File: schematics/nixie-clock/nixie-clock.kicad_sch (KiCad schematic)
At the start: 23 parts, among them J1 Jack-DC, SW1 SW_Push, U1 LM317_TO-220, U2 ATmega328P-P, U3 SN74HC595N, U4 SN74HC595N, U5 K155NA1, U6 K155NA1, U7 K155NA1, U8 K155NA1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

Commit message: annotated nixie driver's inputs
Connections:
- net SER2: now also U3.9 (QH')
- net N1A: now reaches U5.3 (A)
- net N1D: now reaches U5.4 (D)
- net N1B: now reaches U5.6 (B)
- net N1C: now reaches U5.7 (C)
- net N3A: now reaches U7.3 (A)
- net N3D: now reaches U7.4 (D)
- net N3B: now reaches U7.6 (B)
- net N3C: now reaches U7.7 (C)
- net N2A: now reaches U6.3 (A)
- net N2D: now reaches U6.4 (D)
- net N2B: now reaches U6.6 (B)
- net N2C: now reaches U6.7 (C)
- net N4A: now reaches U8.3 (A)
- net N4D: now reaches U8.4 (D)
- net N4B: now reaches U8.6 (B)
- net N4C: now reaches U8.7 (C)
- no-connect marks 0 -> 3
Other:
- note added: "5V Voltage regulator"
- note added: "Crystal oscillator"
- note added: "DC Connector"
- note added: "Nixie tubes and driver circuits"
- note added: "Reset button"
- moved on the sheet: BZ1, C1, C2, C3, C4, J1, N1, N2, N3, N4, R1, R2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

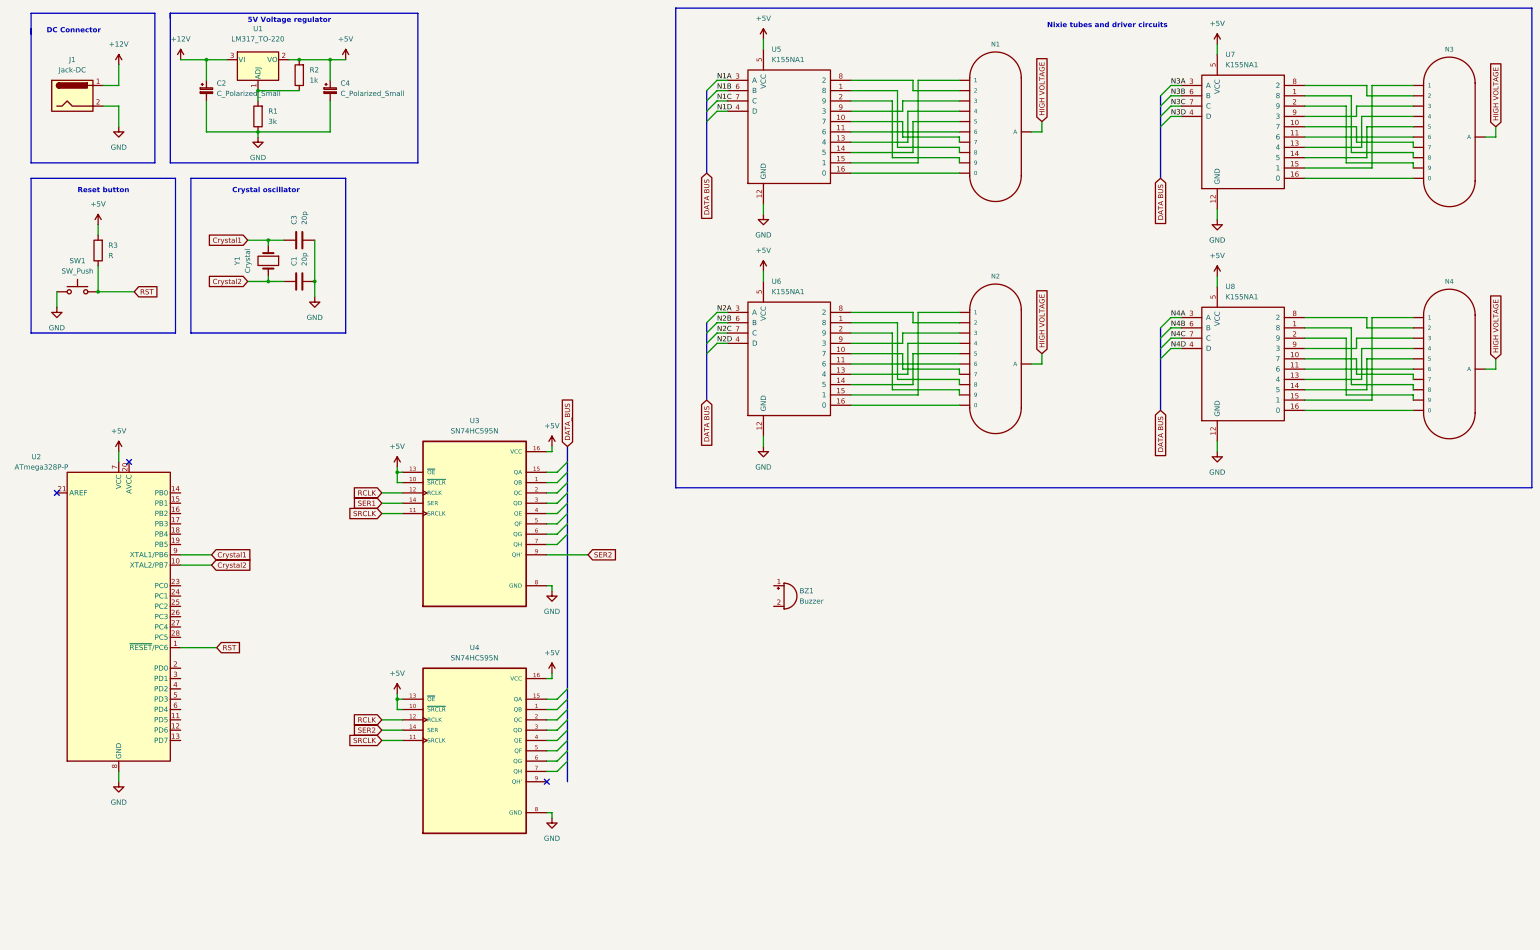
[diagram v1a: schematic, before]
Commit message: schematic: added buttons, rtc, neon bulbs, annotated driver input labels
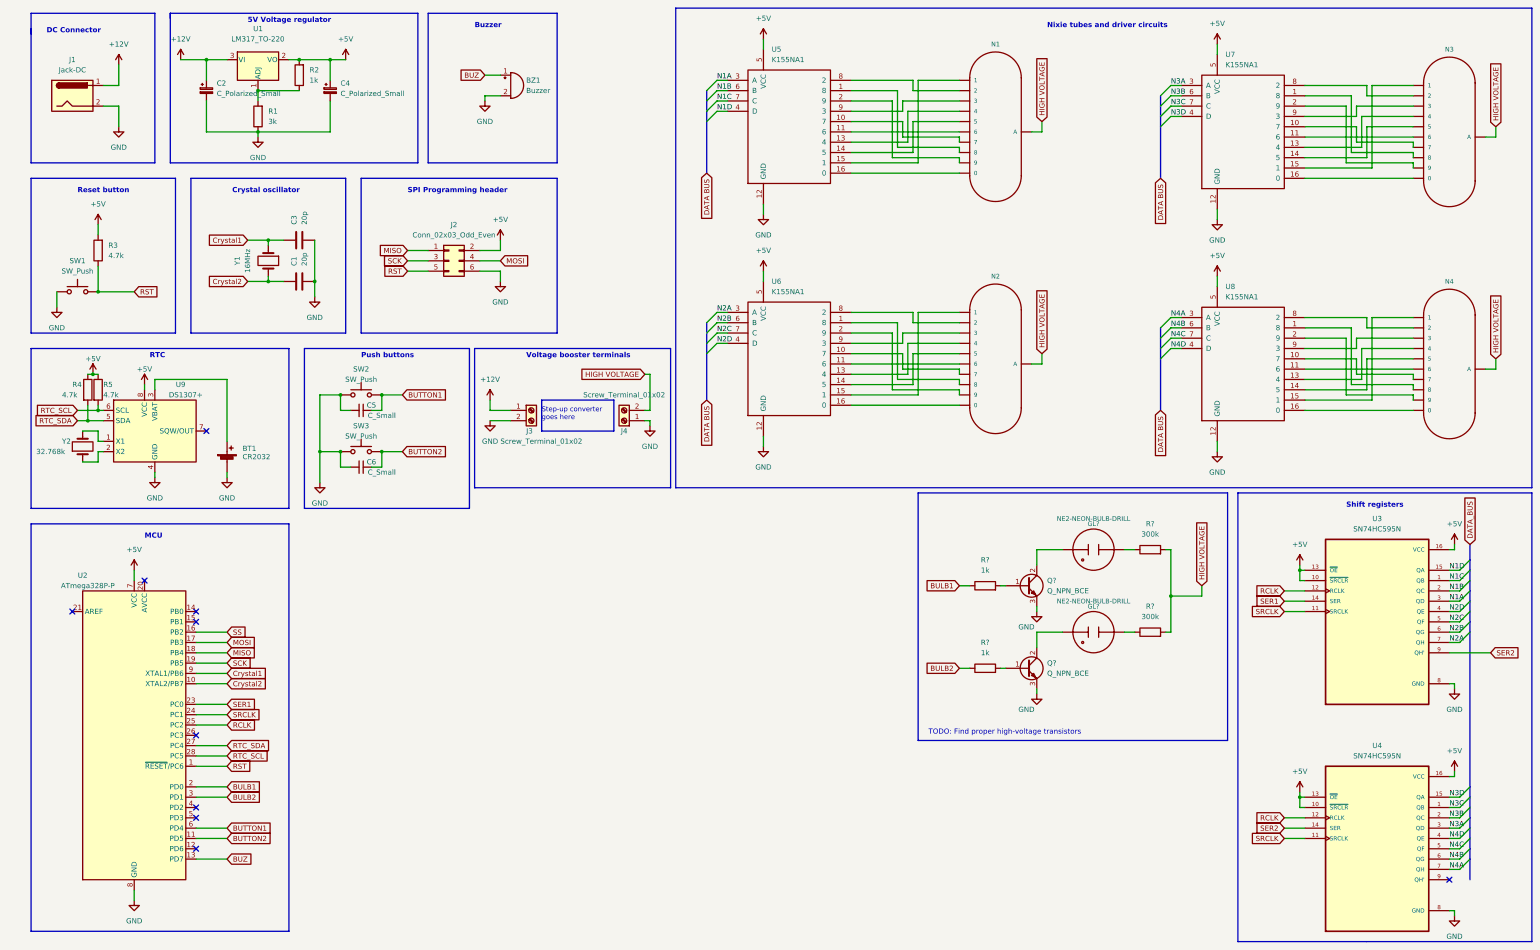
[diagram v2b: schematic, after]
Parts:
- added BT1: CR2032, symbol Device:Battery_Cell
- added C5, C6: C_Small, symbol Device:C_Small
- added GL? (x2): NE2-NEON-BULB-DRILL, mynixies_NE2-NEON-BULB-DRILL, symbol mynixies:NE2-NEON-BULB-DRILL
- added J2: Conn_02x03_Odd_Even, Connector_PinHeader_2.54mm:PinHeader_2x03_P2.54mm_Vertical, symbol Connector_Generic:Conn_02x03_Odd_Even
- added J3, J4: Screw_Terminal_01x02, symbol Connector:Screw_Terminal_01x02
- added Q? (x2): Q_NPN_BCE, symbol Device:Q_NPN_BCE
- added R4, R5: 4.7k, symbol Device:R
- added R? (x2): 1k, symbol Device:R
- added R? (x2): 300k, symbol Device:R
- added SW2, SW3: SW_Push, symbol Switch:SW_Push
- added U9: DS1307+, Package_DIP:DIP-8_W7.62mm, symbol Timer_RTC:DS1307+
- added Y2: 32.768k, symbol Device:Crystal
- N1: footprint nixies-us_IN-1 -> (none)
- R3: value R -> 4.7k
- U5, U6, U7, U8: footprint (none) -> Package_DIP:DIP-14_W7.62mm_Socket
- Y1: value Crystal -> 16MHz
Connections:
- net +12V: now also J3.1 (Pin_1)
- net +5V: now also J2.2 (Pin_2), R4.1, R5.1, U9.8 (VCC)
- net GND: now also BZ1.2 (+), BT1.2 (-), C5.2, C6.2, J2.6 (Pin_6), J3.2 (Pin_2), J4.1 (Pin_1), Q?.3 (E), Q?.3 (E), SW2.1, SW3.1, U9.4 (GND)
- net HIGH VOLTAGE: now also J4.2 (Pin_2), R?.2, R?.2
- net N1A: now also U3.3 (QD)
- net N1B: now also U3.2 (QC)
- net N1C: now also U3.1 (QB)
- net N1D: now also U3.15 (QA)
- net N2A: now also U3.7 (QH)
- net N2B: now also U3.6 (QG)
- net N2C: now also U3.5 (QF)
- net N2D: now also U3.4 (QE)
- net N3A: now also U4.3 (QD)
- net N3B: now also U4.2 (QC)
- net N3C: now also U4.1 (QB)
- net N3D: now also U4.15 (QA)
- net N4A: now also U4.7 (QH)
- net N4B: now also U4.6 (QG)
- net N4C: now also U4.5 (QF)
- net N4D: now also U4.4 (QE)
- net RCLK: now also U2.25 (PC2)
- net RST: now also J2.5 (Pin_5)
- net SER1: now also U2.23 (PC0)
- net SRCLK: now also U2.24 (PC1)
- net BUZ: now reaches BZ1.1 (-)
- net BUZ: now also U2.13 (PD7)
- net BUTTON2: now reaches U2.11 (PD5)
- net BUTTON2: now also C6.1, SW3.2
- net SS: now reaches U2.16 (PB2)
- net MOSI: now reaches U2.17 (PB3)
- net MOSI: now also J2.4 (Pin_4)
- net MISO: now reaches U2.18 (PB4)
- net MISO: now also J2.1 (Pin_1)
- net SCK: now reaches U2.19 (PB5)
- net SCK: now also J2.3 (Pin_3)
- net BULB1: now reaches U2.2 (PD0)
- net BULB1: now also R?.1
- net RTC_SDA: now reaches U2.27 (PC4)
- net RTC_SDA: now also R4.2, U9.5 (SDA)
- net RTC_SCL: now reaches U2.28 (PC5)
- net RTC_SCL: now also R5.2, U9.6 (SCL)
- net BULB2: now reaches U2.3 (PD1)
- net BULB2: now also R?.1
- net BUTTON1: now reaches U2.6 (PD4)
- net BUTTON1: now also C5.1, SW2.2
- new net: BT1.1 (+), U9.3 (VBAT)
- new net: Q?.1 (B), R?.2 (x2)
- new net: GL?.1 (A), R?.1 (x2)
- new net: GL?.2 (A1), Q?.2 (C) (x2)
- new net: U9.1 (X1), Y2.2
- new net: U9.2 (X2), Y2.1
- no-connect marks 3 -> 10
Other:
- note added: "Buzzer"
- note added: "MCU"
- note added: "Push buttons"
- note added: "RTC"
- note added: "SPI Programming header"
- note added: "Shift registers"
- note added: "Step-up converter goes here"
- note added: "TODO: Find proper high-voltage transistors"
- note added: "Voltage booster terminals"
- moved on the sheet: BZ1, U2, U3, U4

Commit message: schematic: corrected k155id1's pinout to dip16 instead of 14
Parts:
- GL? (x2): value NE2-NEON-BULB-DRILL -> INS-1
- U5, U6, U7, U8: value K155NA1 -> K155ID1; footprint Package_DIP:DIP-14_W7.62mm_Socket -> Package_DIP:DIP-16_W7.62mm_Socket
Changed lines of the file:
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@@
       (effects (font (size 1.27 1.27)) (justify left))
     )
-    (property "Value" "K155NA1" (id 1) (at 207.7594 34.29 0)
-      (effects (font (size 1.27 1.27)) (justify left))
-    )
-    (property "Footprint" "Package_DIP:DIP-14_W7.62mm_Socket" (id 2) (at 212.09 50.8 0)
+    (property "Value" "K155ID1" (id 1) (at 207.7594 34.29 0)
+      (effects (font (size 1.27 1.27)) (justify left))
+    )
+    (property "Footprint" "Package_DIP:DIP-16_W7.62mm_Socket" (id 2) (at 212.09 50.8 0)
       (effects (font (size 1.27 1.27)) hide)
     )
@@
       (effects (font (size 1.143 1.143)))
     )
-    (property "Value" "NE2-NEON-BULB-DRILL" (id 1) (at 287.02 147.32 90)
+    (property "Value" "INS-1" (id 1) (at 287.02 161.29 90)
       (effects (font (size 1.143 1.143)))
     )
@@
       (effects (font (size 1.27 1.27)) (justify left))
     )
-    (property "Value" "K155NA1" (id 1) (at 319.5194 35.56 0)
-      (effects (font (size 1.27 1.27)) (justify left))
-    )
-    (property "Footprint" "Package_DIP:DIP-14_W7.62mm_Socket" (id 2) (at 323.85 52.07 0)
+    (property "Value" "K155ID1" (id 1) (at 319.5194 35.56 0)
+      (effects (font (size 1.27 1.27)) (justify left))
+    )
+    (property "Footprint" "Package_DIP:DIP-16_W7.62mm_Socket" (id 2) (at 323.85 52.07 0)
       (effects (font (size 1.27 1.27)) hide)
     )
@@
       (effects (font (size 1.27 1.27)) (justify left))
     )
-    (property "Value" "K155NA1" (id 1) (at 207.7594 91.44 0)
-      (effects (font (size 1.27 1.27)) (justify left))
-    )
-    (property "Footprint" "Package_DIP:DIP-14_W7.62mm_Socket" (id 2) (at 212.09 107.95 0)
+    (property "Value" "K155ID1" (id 1) (at 207.7594 91.44 0)
+      (effects (font (size 1.27 1.27)) (justify left))
+    )
+    (property "Footprint" "Package_DIP:DIP-16_W7.62mm_Socket" (id 2) (at 212.09 107.95 0)
       (effects (font (size 1.27 1.27)) hide)
     )
@@
       (effects (font (size 1.27 1.27)) (justify left))
     )
-    (property "Value" "K155NA1" (id 1) (at 319.5194 92.71 0)
-      (effects (font (size 1.27 1.27)) (justify left))
-    )
-    (property "Footprint" "Package_DIP:DIP-14_W7.62mm_Socket" (id 2) (at 323.85 109.22 0)
+    (property "Value" "K155ID1" (id 1) (at 319.5194 92.71 0)
+      (effects (font (size 1.27 1.27)) (justify left))
+    )
+    (property "Footprint" "Package_DIP:DIP-16_W7.62mm_Socket" (id 2) (at 323.85 109.22 0)
       (effects (font (size 1.27 1.27)) hide)
     )
@@
       (effects (font (size 1.143 1.143)))
     )
-    (property "Value" "NE2-NEON-BULB-DRILL" (id 1) (at 287.02 167.64 90)
+    (property "Value" "INS-1" (id 1) (at 287.02 181.61 90)
       (effects (font (size 1.143 1.143)))
     )
@@
     )
     (path "/345e2975-581d-4a8c-8af1-443eac8fd640"
-      (reference "GL?") (unit 1) (value "NE2-NEON-BULB-DRILL") (footprint "mynixies_NE2-NEON-BULB-DRILL")
+      (reference "GL?") (unit 1) (value "INS-1") (footprint "mynixies_NE2-NEON-BULB-DRILL")
     )
     (path "/fbf9fc96-43f5-4a53-be4f-0f9323bfd90c"
-      (reference "GL?") (unit 1) (value "NE2-NEON-BULB-DRILL") (footprint "mynixies_NE2-NEON-BULB-DRILL")
+      (reference "GL?") (unit 1) (value "INS-1") (footprint "mynixies_NE2-NEON-BULB-DRILL")
     )
     (path "/2f3c2211-6c84-4020-a1b4-5759bcf85a5c"
@@
     )
     (path "/04d182f1-d009-49f3-b3e6-b46d9a90aa92"
-      (reference "U5") (unit 1) (value "K155NA1") (footprint "Package_DIP:DIP-14_W7.62mm_Socket")
+      (reference "U5") (unit 1) (value "K155ID1") (footprint "Package_DIP:DIP-16_W7.62mm_Socket")
     )
     (path "/64e8c480-67c5-45e2-9eb8-ede62713c06f"
-      (reference "U6") (unit 1) (value "K155NA1") (footprint "Package_DIP:DIP-14_W7.62mm_Socket")
+      (reference "U6") (unit 1) (value "K155ID1") (footprint "Package_DIP:DIP-16_W7.62mm_Socket")
     )
     (path "/52613085-5931-49fd-bd52-08509dc07be3"
-      (reference "U7") (unit 1) (value "K155NA1") (footprint "Package_DIP:DIP-14_W7.62mm_Socket")
+      (reference "U7") (unit 1) (value "K155ID1") (footprint "Package_DIP:DIP-16_W7.62mm_Socket")
     )
     (path "/d2a2bba5-d132-4e9e-a70e-8efe18d0ccab"
-      (reference "U8") (unit 1) (value "K155NA1") (footprint "Package_DIP:DIP-14_W7.62mm_Socket")
+      (reference "U8") (unit 1) (value "K155ID1") (footprint "Package_DIP:DIP-16_W7.62mm_Socket")
     )
     (path "/9173ca2e-fc04-4e30-a9da-4da9d615bc48"

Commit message: schematic: added in-1 footprint from included library
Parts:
- N1: footprint (none) -> nixies-us:nixies-us-IN-1
- N2, N3, N4: footprint nixies-us_IN-1 -> nixies-us:nixies-us-IN-1
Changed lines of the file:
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@@
       (effects (font (size 1.143 1.143)) (justify left bottom) hide)
     )
-    (property "Footprint" "nixies-us_IN-1" (id 2) (at 264.922 105.41 0)
+    (property "Footprint" "nixies-us:nixies-us-IN-1" (id 2) (at 264.922 105.41 0)
       (effects (font (size 0.508 0.508)) hide)
     )
@@
       (effects (font (size 1.143 1.143)) (justify left bottom) hide)
     )
-    (property "Footprint" "nixies-us_IN-1" (id 2) (at 376.682 106.68 0)
+    (property "Footprint" "nixies-us:nixies-us-IN-1" (id 2) (at 376.682 106.68 0)
       (effects (font (size 0.508 0.508)) hide)
     )
@@
       (effects (font (size 1.143 1.143)) (justify left bottom) hide)
     )
-    (property "Footprint" "" (id 2) (at 264.922 48.26 0)
+    (property "Footprint" "nixies-us:nixies-us-IN-1" (id 2) (at 264.922 48.26 0)
       (effects (font (size 0.508 0.508)) hide)
     )
@@
       (effects (font (size 1.143 1.143)) (justify left bottom) hide)
     )
-    (property "Footprint" "nixies-us_IN-1" (id 2) (at 376.682 49.53 0)
+    (property "Footprint" "nixies-us:nixies-us-IN-1" (id 2) (at 376.682 49.53 0)
       (effects (font (size 0.508 0.508)) hide)
     )
@@
     )
     (path "/819cd935-2cda-47a0-b6b4-1364c82c84b7"
-      (reference "N1") (unit 1) (value "IN-1") (footprint "")
+      (reference "N1") (unit 1) (value "IN-1") (footprint "nixies-us:nixies-us-IN-1")
     )
     (path "/2f78acd8-feba-4edb-a624-ff5c6af6307b"
-      (reference "N2") (unit 1) (value "IN-1") (footprint "nixies-us_IN-1")
+      (reference "N2") (unit 1) (value "IN-1") (footprint "nixies-us:nixies-us-IN-1")
     )
     (path "/aa35d094-0eb9-45cb-bb2e-b75cdebf8981"
-      (reference "N3") (unit 1) (value "IN-1") (footprint "nixies-us_IN-1")
+      (reference "N3") (unit 1) (value "IN-1") (footprint "nixies-us:nixies-us-IN-1")
     )
     (path "/61e30a05-e9e6-460b-9a1c-8c82888c9101"
-      (reference "N4") (unit 1) (value "IN-1") (footprint "nixies-us_IN-1")
+      (reference "N4") (unit 1) (value "IN-1") (footprint "nixies-us:nixies-us-IN-1")
     )
     (path "/6b209868-a479-492e-ad24-e544bd17597a"

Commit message: annotated components, added footprints to most caps and ICs
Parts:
- removed C2, C4: C_Polarized_Small, symbol Device:C_Polarized_Small
- removed J1: Jack-DC, symbol Connector:Jack-DC
- added C1: 4.7u, Capacitor_SMD:C_0805_2012Metric_Pad1.18x1.45mm_HandSolder, symbol Device:C_Small
- added C2: 10u, symbol Device:C_Small
- added C5: 10u, symbol Device:C_Polarized
- added C6: 100n, Capacitor_SMD:C_0805_2012Metric_Pad1.18x1.45mm_HandSolder, symbol Device:C
- added J1: Barrel_Jack_Switch, Connector_BarrelJack:BarrelJack_Wuerth_6941xx301002, symbol Connector:Barrel_Jack_Switch
- added R6: 1k, symbol Device:R
- BT1: footprint (none) -> Battery:BatteryHolder_Keystone_1060_1x2032
- BZ1: footprint (none) -> Buzzer_Beeper:Buzzer_12x9.5RM7.6
- C3: footprint (none) -> Capacitor_SMD:C_0603_1608Metric_Pad1.08x0.95mm_HandSolder
- C4: renamed from C1; footprint (none) -> Capacitor_SMD:C_0603_1608Metric_Pad1.08x0.95mm_HandSolder
- C7: renamed from C5; value C_Small -> 100n; footprint (none) -> Capacitor_SMD:C_0805_2012Metric_Pad1.18x1.45mm_HandSolder
- C8: renamed from C6; value C_Small -> 100n; footprint (none) -> Capacitor_SMD:C_0805_2012Metric_Pad1.18x1.45mm_HandSolder
- U3, U4: footprint DIP794W45P254L1969H508Q16 -> SN74HC595N:DIP794W45P254L1969H508Q16
- Y1: footprint (none) -> Crystal:Crystal_HC49-U_Vertical
- Y2: footprint (none) -> Crystal:Crystal_DS26_D2.0mm_L6.0mm_Horizontal
- gave numbers to parts that had none: 8
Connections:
- net +12V: now also C1.1, J1.1
- net +5V: now also C2.1, C5.1, C6.1, R6.1
- net GND: now also C1.2, C2.2, C5.2, C6.2, J1.2, R6.2
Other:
- note added: "MCU power filtering"
- note added: "NOTE: keep close to MCU"
- note added: "NOTE: keep close to MCU and surround with ground plane"
- note added: "NOTE: test those cap values later"
- note added: "Neon bulbs"
- company: (none) -> KNE AGH, Kacper Filipek
- title: (none) -> Nixie Clock
- moved on the sheet: C3, C4, R1, R2, U1, Y1

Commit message: schematic: added transistor model
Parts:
- Q1, Q2: value Q_NPN_BCE -> MJE13007; footprint (none) -> Package_TO_SOT_THT:TO-220-3_Vertical
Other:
- note removed: "TODO: Find proper high-voltage transistors"
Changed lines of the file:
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@@
     (effects (font (size 1.27 1.27) bold) (justify left bottom))
-  )
-  (text "TODO: Find proper high-voltage transistors" (at 246.38 200.66 0)
-    (effects (font (size 1.27 1.27)) (justify left bottom))
   )
   (label "N3B" (at 374.65 220.98 0)
@@
       (effects (font (size 1.27 1.27)) (justify left))
     )
-    (property "Value" "Q_NPN_BCE" (id 1) (at 275.59 165.0999 0)
-      (effects (font (size 1.27 1.27)) (justify left))
-    )
-    (property "Footprint" "" (id 2) (at 275.59 161.29 0)
+    (property "Value" "MJE13007" (id 1) (at 275.59 165.0999 0)
+      (effects (font (size 1.27 1.27)) (justify left))
+    )
+    (property "Footprint" "Package_TO_SOT_THT:TO-220-3_Vertical" (id 2) (at 275.59 161.29 0)
       (effects (font (size 1.27 1.27)) hide)
     )
@@
       (effects (font (size 1.27 1.27)) (justify left))
     )
-    (property "Value" "Q_NPN_BCE" (id 1) (at 275.59 185.4199 0)
-      (effects (font (size 1.27 1.27)) (justify left))
-    )
-    (property "Footprint" "" (id 2) (at 275.59 181.61 0)
+    (property "Value" "MJE13007" (id 1) (at 275.59 185.4199 0)
+      (effects (font (size 1.27 1.27)) (justify left))
+    )
+    (property "Footprint" "Package_TO_SOT_THT:TO-220-3_Vertical" (id 2) (at 275.59 181.61 0)
       (effects (font (size 1.27 1.27)) hide)
     )
@@
     )
     (path "/6b209868-a479-492e-ad24-e544bd17597a"
-      (reference "Q1") (unit 1) (value "Q_NPN_BCE") (footprint "")
+      (reference "Q1") (unit 1) (value "MJE13007") (footprint "Package_TO_SOT_THT:TO-220-3_Vertical")
     )
     (path "/aaa54154-8446-4a77-b89e-aec4b24b1268"
-      (reference "Q2") (unit 1) (value "Q_NPN_BCE") (footprint "")
+      (reference "Q2") (unit 1) (value "MJE13007") (footprint "Package_TO_SOT_THT:TO-220-3_Vertical")
     )
     (path "/b03cdc92-7820-44a0-990b-ce60455c7389"

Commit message: schematic: assigned all footprints, schematic finished (i hope)
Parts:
- removed C5: 10u, symbol Device:C_Polarized
- removed GL1, GL2: INS-1, mynixies_NE2-NEON-BULB-DRILL, symbol mynixies:NE2-NEON-BULB-DRILL
- added N5, N6: INS-1, mynixies:mynixies-INS-1, symbol mynixies:INS-1
- C2: footprint (none) -> Capacitor_SMD:C_0805_2012Metric_Pad1.18x1.45mm_HandSolder
- J3, J4: footprint (none) -> TerminalBlock_Phoenix:TerminalBlock_Phoenix_MKDS-1,5-2_1x02_P5.00mm_Horizontal
- R1, R10, R2, R3, R4, R5, R6, R7, R8, R9: footprint (none) -> Resistor_SMD:R_0805_2012Metric_Pad1.20x1.40mm_HandSolder
- SW1: footprint (none) -> Button_Switch_THT:SW_PUSH_6mm_H13mm
- SW2, SW3: footprint (none) -> Button_Switch_Keyboard:SW_Cherry_MX_1.00u_PCB
- renumbered C6 to C5
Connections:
- net at R9.1: now also N5.P$2 (A)
- net at Q1.2 (C): now also N5.P$1 (C)
- net at R10.1: now also N6.P$2 (A)
- net at Q2.2 (C): now also N6.P$1 (C)
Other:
- moved on the sheet: C5, R3, SW1
